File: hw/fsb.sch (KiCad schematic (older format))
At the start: 11 parts, among them J101 AMPSEAL_8_POS_VERT_WHITE_SEAL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, J102 AMPSEAL_23_POS_VERT_WHITE_SEA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

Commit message: last modifications to 3.0.0
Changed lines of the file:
@@
 F21 "DOORSW2" I L 4250 5050 60
 F22 "SEATSW" I L 4250 4700 60
+F23 "HEATER_PWM" O R 6400 5200 50
 $EndSheet
 $Comp
@@
 Text Label 9550 5200 0    50   ~ 0
 HEATER_15-
+Wire Wire Line
+	6400 5200 8500 5200
 $EndSCHEMATC

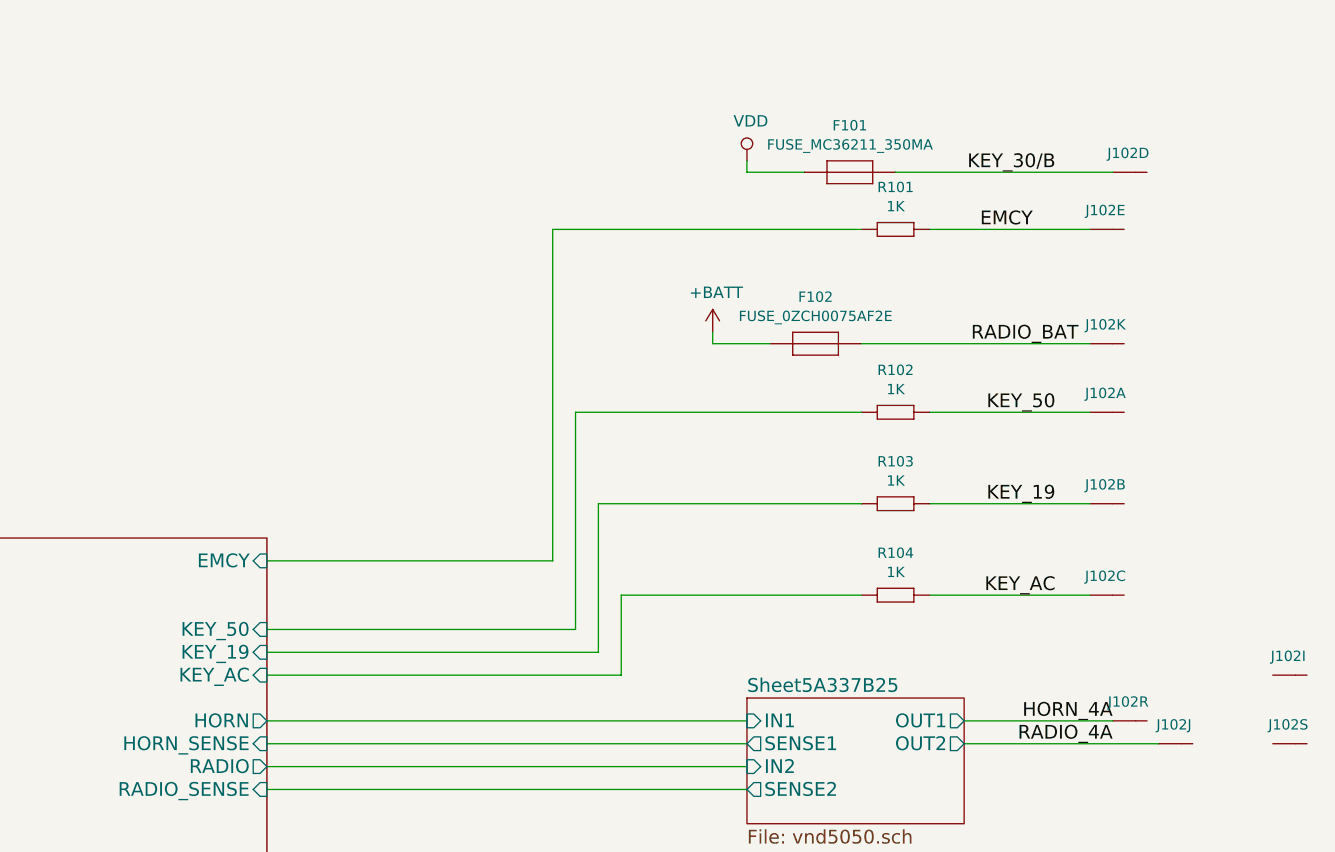
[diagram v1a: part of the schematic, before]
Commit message: hw 3.1.0 created. Fuel level moved from esb to fsb
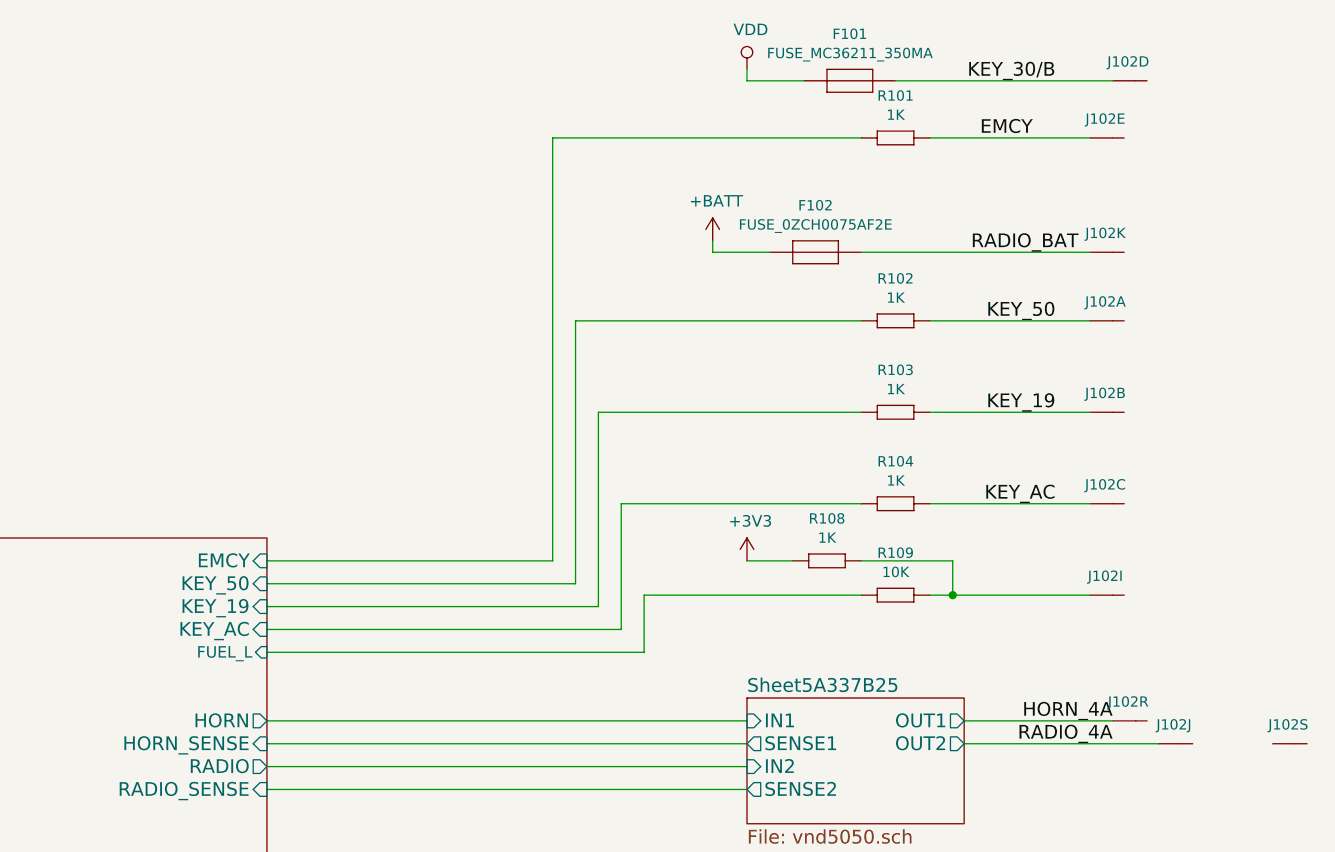
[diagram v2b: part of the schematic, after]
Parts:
- added R108: 1K, yageo:0603, symbol fsb-rescue:1K
- added R109: 10K, yageo:0603, symbol fsb-rescue:10K
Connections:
- net +3V3: now also R108.1 (R1)
- net at J102.P$9 (S): now also R108.2 (R2), R109.1 (R1)
- new net LPC1549/FUEL_L: R109.2 (R2)
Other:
- moved on the sheet: F101, F102, J102A, J102B, J102C, J102D, J102E, J102I, J102K, R101, R102, R103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

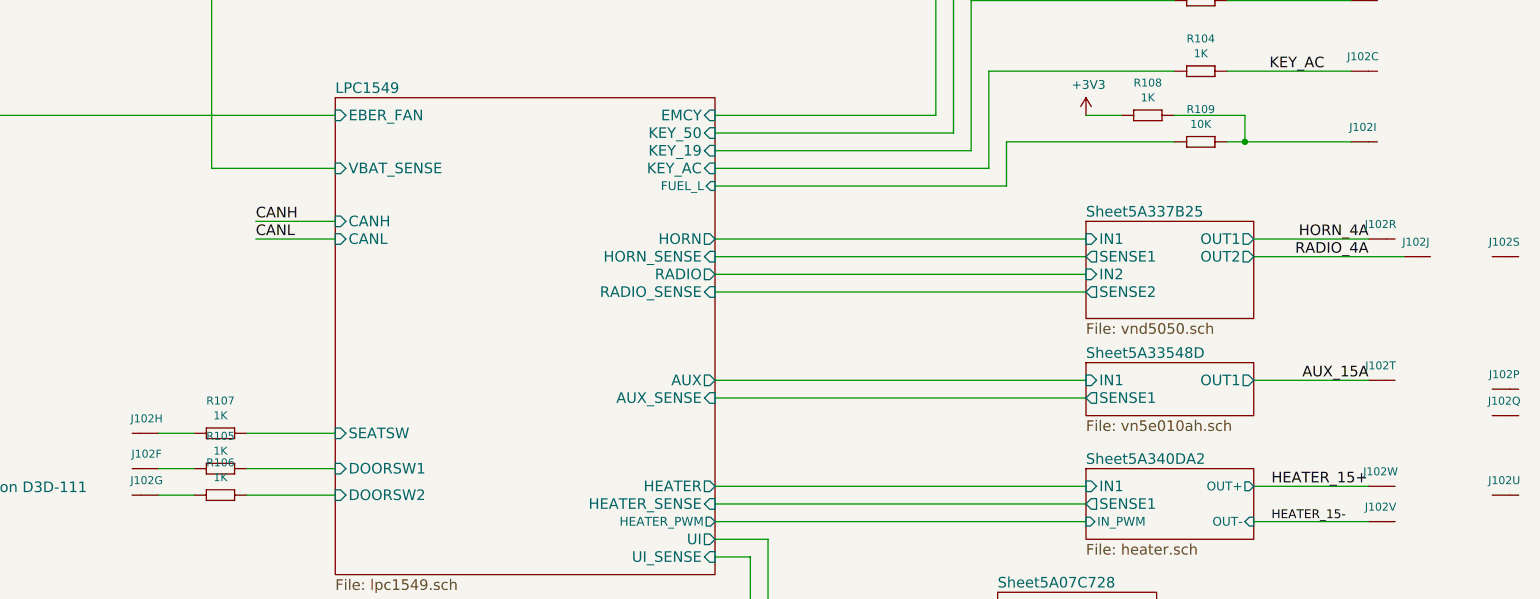
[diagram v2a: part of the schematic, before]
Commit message: 4.1.0 pcb ordered, with modified flyback diodes
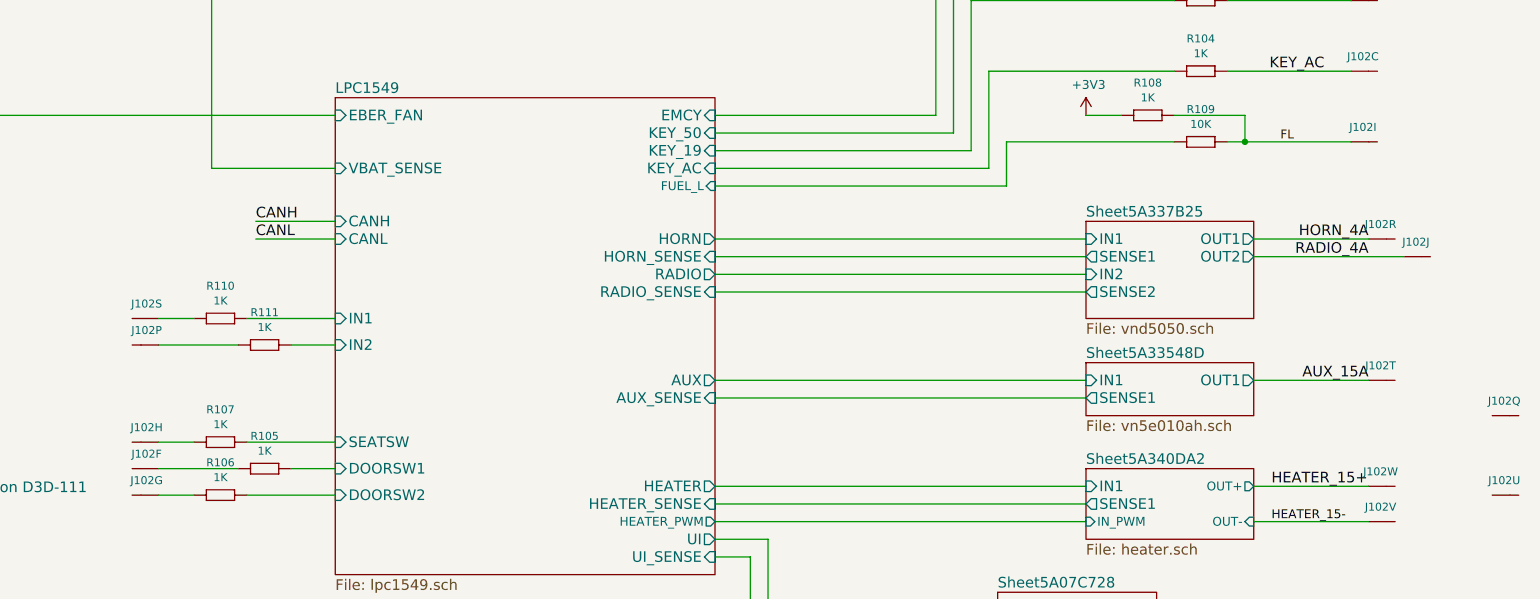
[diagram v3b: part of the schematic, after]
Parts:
- added R110, R111: 1K, yageo:0603, symbol fsb-rescue:1K
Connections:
- net FL: now reaches J102.P$9 (S), R108.2 (R2), R109.1 (R1)
- net at J102.P$16 (S): now also R111.2 (R2)
- net at J102.P$19 (S): now also R110.2 (R2)
- new net LPC1549/IN1: R110.1 (R1)
- new net LPC1549/IN2: R111.1 (R1)
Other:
- moved on the sheet: J102H, J102P, J102S, R105, R107
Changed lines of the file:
@@
 F20 "DOORSW1" I L 4250 4900 60
 F21 "DOORSW2" I L 4250 5050 60
-F22 "SEATSW" I L 4250 4700 60
+F22 "SEATSW" I L 4250 4750 60
 F23 "HEATER_PWM" O R 6400 5200 50
 F24 "FUEL_L" I R 6400 3300 50
+F25 "IN1" I L 4250 4050 60
+F26 "IN2" I L 4250 4200 60
 $EndSheet
 $Comp
@@
 L fsb-rescue:AMPSEAL_23_POS_VERT_WHITE_SEALED_1-776228-2-RESCUE-fsb J102
 U 8 1 5988B38C
-P 3150 4700
-F 0 "J102" H 3118 4783 45  0000 C CNN
-F 1 "AMPSEAL_23_POS_VERT_WHITE_SEALED_1-776228-2" H 3150 4700 45  0001 L BNN
-F 2 "usevolt:AMPSEAL_23_POS_776200-1" H 3180 4850 20  0001 C CNN
-F 3 "http://www.mouser.com/ds/2/418/NG_CD_776228_C13-692101.pdf" H 3250 4670 60  0001 C CNN
-F 4 "571-1-776228-2" H 3650 5070 60  0001 C CNN "1st Source Part Number"
-F 5 "1-776228-2" H 3450 4870 60  0001 C CNN "Manufacturer Part Number"
-F 6 "Mouser" H 3550 4970 60  0001 C CNN "1st Source"
-F 7 "TE Connectivity" H 3350 4770 60  0001 C CNN "Manufacturer"
-	8    3150 4700
+P 3150 4750
+F 0 "J102" H 3118 4833 45  0000 C CNN
+F 1 "AMPSEAL_23_POS_VERT_WHITE_SEALED_1-776228-2" H 3150 4750 45  0001 L BNN
+F 2 "usevolt:AMPSEAL_23_POS_776200-1" H 3180 4900 20  0001 C CNN
+F 3 "http://www.mouser.com/ds/2/418/NG_CD_776228_C13-692101.pdf" H 3250 4720 60  0001 C CNN
+F 4 "571-1-776228-2" H 3650 5120 60  0001 C CNN "1st Source Part Number"
+F 5 "1-776228-2" H 3450 4920 60  0001 C CNN "Manufacturer Part Number"
+F 6 "Mouser" H 3550 5020 60  0001 C CNN "1st Source"
+F 7 "TE Connectivity" H 3350 4820 60  0001 C CNN "Manufacturer"
+	8    3150 4750
 	-1   0    0    -1
 $EndComp
@@
 L fsb-rescue:AMPSEAL_23_POS_VERT_WHITE_SEALED_1-776228-2-RESCUE-fsb J102
 U 16 1 5988B7B4
-P 10900 4450
-F 0 "J102" H 10868 4533 45  0000 C CNN
-F 1 "AMPSEAL_23_POS_VERT_WHITE_SEALED_1-776228-2" H 10900 4450 45  0001 L BNN
-F 2 "usevolt:AMPSEAL_23_POS_776200-1" H 10930 4600 20  0001 C CNN
-F 3 "http://www.mouser.com/ds/2/418/NG_CD_776228_C13-692101.pdf" H 11000 4420 60  0001 C CNN
-F 4 "571-1-776228-2" H 11400 4820 60  0001 C CNN "1st Source Part Number"
-F 5 "1-776228-2" H 11200 4620 60  0001 C CNN "Manufacturer Part Number"
-F 6 "Mouser" H 11300 4720 60  0001 C CNN "1st Source"
-F 7 "TE Connectivity" H 11100 4520 60  0001 C CNN "Manufacturer"
-	16   10900 4450
-	1    0    0    -1
+P 3150 4200
+F 0 "J102" H 3118 4283 45  0000 C CNN
+F 1 "AMPSEAL_23_POS_VERT_WHITE_SEALED_1-776228-2" H 3150 4200 45  0001 L BNN
+F 2 "usevolt:AMPSEAL_23_POS_776200-1" H 3180 4350 20  0001 C CNN
+F 3 "http://www.mouser.com/ds/2/418/NG_CD_776228_C13-692101.pdf" H 3250 4170 60  0001 C CNN
+F 4 "571-1-776228-2" H 3650 4570 60  0001 C CNN "1st Source Part Number"
+F 5 "1-776228-2" H 3450 4370 60  0001 C CNN "Manufacturer Part Number"
+F 6 "Mouser" H 3550 4470 60  0001 C CNN "1st Source"
+F 7 "TE Connectivity" H 3350 4270 60  0001 C CNN "Manufacturer"
+	16   3150 4200
+	-1   0    0    -1
 $EndComp
 $Comp
@@
 L fsb-rescue:AMPSEAL_23_POS_VERT_WHITE_SEALED_1-776228-2-RESCUE-fsb J102
 U 19 1 5988C267
-P 10900 3700
-F 0 "J102" H 10868 3783 45  0000 C CNN
-F 1 "AMPSEAL_23_POS_VERT_WHITE_SEALED_1-776228-2" H 10900 3700 45  0001 L BNN
-F 2 "usevolt:AMPSEAL_23_POS_776200-1" H 10930 3850 20  0001 C CNN
-F 3 "http://www.mouser.com/ds/2/418/NG_CD_776228_C13-692101.pdf" H 11000 3670 60  0001 C CNN
-F 4 "571-1-776228-2" H 11400 4070 60  0001 C CNN "1st Source Part Number"
-F 5 "1-776228-2" H 11200 3870 60  0001 C CNN "Manufacturer Part Number"
-F 6 "Mouser" H 11300 3970 60  0001 C CNN "1st Source"
-F 7 "TE Connectivity" H 11100 3770 60  0001 C CNN "Manufacturer"
-	19   10900 3700
-	1    0    0    -1
+P 3150 4050
+F 0 "J102" H 3118 4133 45  0000 C CNN
+F 1 "AMPSEAL_23_POS_VERT_WHITE_SEALED_1-776228-2" H 3150 4050 45  0001 L BNN
+F 2 "usevolt:AMPSEAL_23_POS_776200-1" H 3180 4200 20  0001 C CNN
+F 3 "http://www.mouser.com/ds/2/418/NG_CD_776228_C13-692101.pdf" H 3250 4020 60  0001 C CNN
+F 4 "571-1-776228-2" H 3650 4420 60  0001 C CNN "1st Source Part Number"
+F 5 "1-776228-2" H 3450 4220 60  0001 C CNN "Manufacturer Part Number"
+F 6 "Mouser" H 3550 4320 60  0001 C CNN "1st Source"
+F 7 "TE Connectivity" H 3350 4120 60  0001 C CNN "Manufacturer"
+	19   3150 4050
+	-1   0    0    -1
 $EndComp
 $Comp
@@
 	4250 5050 3750 5050
 Wire Wire Line
-	3750 4900 4250 4900
+	4000 4900 4250 4900
 $Comp
 L fsb-rescue:1K R105
 U 1 1 5A09BE6F
-P 3550 4900
-F 0 "R105" H 3600 5084 45  0000 C CNN
-F 1 "1K" H 3600 5000 45  0000 C CNN
-F 2 "yageo:0603" H 3580 5050 20  0001 C CNN
-F 3 "" H 3519 4939 60  0001 C CNN
-F 4 "" H 3919 5339 60  0001 C CNN "1st Source Part Number"
-F 5 "Digikey" H 3819 5239 60  0001 C CNN "1st Source"
-F 6 "RC0603FR-071KL" H 3719 5139 60  0001 C CNN "Manufacturer Part Number"
-F 7 "YAGEO" H 3619 5039 60  0001 C CNN "Manufacturer"
-	1    3550 4900
+P 3800 4900
+F 0 "R105" H 3850 5084 45  0000 C CNN
+F 1 "1K" H 3850 5000 45  0000 C CNN
+F 2 "yageo:0603" H 3830 5050 20  0001 C CNN
+F 3 "" H 3769 4939 60  0001 C CNN
+F 4 "" H 4169 5339 60  0001 C CNN "1st Source Part Number"
+F 5 "Digikey" H 4069 5239 60  0001 C CNN "1st Source"
+F 6 "RC0603FR-071KL" H 3969 5139 60  0001 C CNN "Manufacturer Part Number"
+F 7 "YAGEO" H 3869 5039 60  0001 C CNN "Manufacturer"
+	1    3800 4900
 	1    0    0    -1
 $EndComp
@@
 $EndComp
 Wire Wire Line
-	3450 4900 3250 4900
+	3700 4900 3250 4900
 Wire Wire Line
 	3250 5050 3450 5050
@@
 $EndSheet
 Wire Wire Line
-	3750 4700 4250 4700
+	3750 4750 4250 4750
 $Comp
 L fsb-rescue:1K R107
 U 1 1 5A33C203
-P 3550 4700
-F 0 "R107" H 3600 4884 45  0000 C CNN
-F 1 "1K" H 3600 4800 45  0000 C CNN
-F 2 "yageo:0603" H 3580 4850 20  0001 C CNN
-F 3 "" H 3519 4739 60  0001 C CNN
-F 4 "" H 3919 5139 60  0001 C CNN "1st Source Part Number"
-F 5 "Digikey" H 3819 5039 60  0001 C CNN "1st Source"
-F 6 "RC0603FR-071KL" H 3719 4939 60  0001 C CNN "Manufacturer Part Number"
-F 7 "YAGEO" H 3619 4839 60  0001 C CNN "Manufacturer"
-	1    3550 4700
-	1    0    0    -1
-$EndComp
-Wire Wire Line
-	3450 4700 3250 4700
+P 3550 4750
+F 0 "R107" H 3600 4934 45  0000 C CNN
+F 1 "1K" H 3600 4850 45  0000 C CNN
+F 2 "yageo:0603" H 3580 4900 20  0001 C CNN
+F 3 "" H 3519 4789 60  0001 C CNN
+F 4 "" H 3919 5189 60  0001 C CNN "1st Source Part Number"
+F 5 "Digikey" H 3819 5089 60  0001 C CNN "1st Source"
+F 6 "RC0603FR-071KL" H 3719 4989 60  0001 C CNN "Manufacturer Part Number"
+F 7 "YAGEO" H 3619 4889 60  0001 C CNN "Manufacturer"
+	1    3550 4750
+	1    0    0    -1
+$EndComp
+Wire Wire Line
+	3450 4750 3250 4750
 $Sheet
 S 8500 4900 950  400
@@
 Wire Wire Line
 	8050 3050 9000 3050
+Text Label 9600 3050 0    50   ~ 0
+FL
+$Comp
+L fsb-rescue:1K R111
+U 1 1 5B1711B4
+P 3800 4200
+F 0 "R111" H 3850 4384 45  0000 C CNN
+F 1 "1K" H 3850 4300 45  0000 C CNN
+F 2 "yageo:0603" H 3830 4350 20  0001 C CNN
+F 3 "" H 3769 4239 60  0001 C CNN
+F 4 "" H 4169 4639 60  0001 C CNN "1st Source Part Number"
+F 5 "Digikey" H 4069 4539 60  0001 C CNN "1st Source"
+F 6 "RC0603FR-071KL" H 3969 4439 60  0001 C CNN "Manufacturer Part Number"
+F 7 "YAGEO" H 3869 4339 60  0001 C CNN "Manufacturer"
+	1    3800 4200
+	1    0    0    -1
+$EndComp
+$Comp
+L fsb-rescue:1K R110
+U 1 1 5B1712C5
+P 3550 4050
+F 0 "R110" H 3600 4234 45  0000 C CNN
+F 1 "1K" H 3600 4150 45  0000 C CNN
+F 2 "yageo:0603" H 3580 4200 20  0001 C CNN
+F 3 "" H 3519 4089 60  0001 C CNN
+F 4 "" H 3919 4489 60  0001 C CNN "1st Source Part Number"
+F 5 "Digikey" H 3819 4389 60  0001 C CNN "1st Source"
+F 6 "RC0603FR-071KL" H 3719 4289 60  0001 C CNN "Manufacturer Part Number"
+F 7 "YAGEO" H 3619 4189 60  0001 C CNN "Manufacturer"
+	1    3550 4050
+	1    0    0    -1
+$EndComp
+Wire Wire Line
+	4250 4050 3750 4050
+Wire Wire Line
+	4000 4200 4250 4200
+Wire Wire Line
+	3250 4050 3450 4050
+Wire Wire Line
+	3700 4200 3250 4200
 $EndSCHEMATC

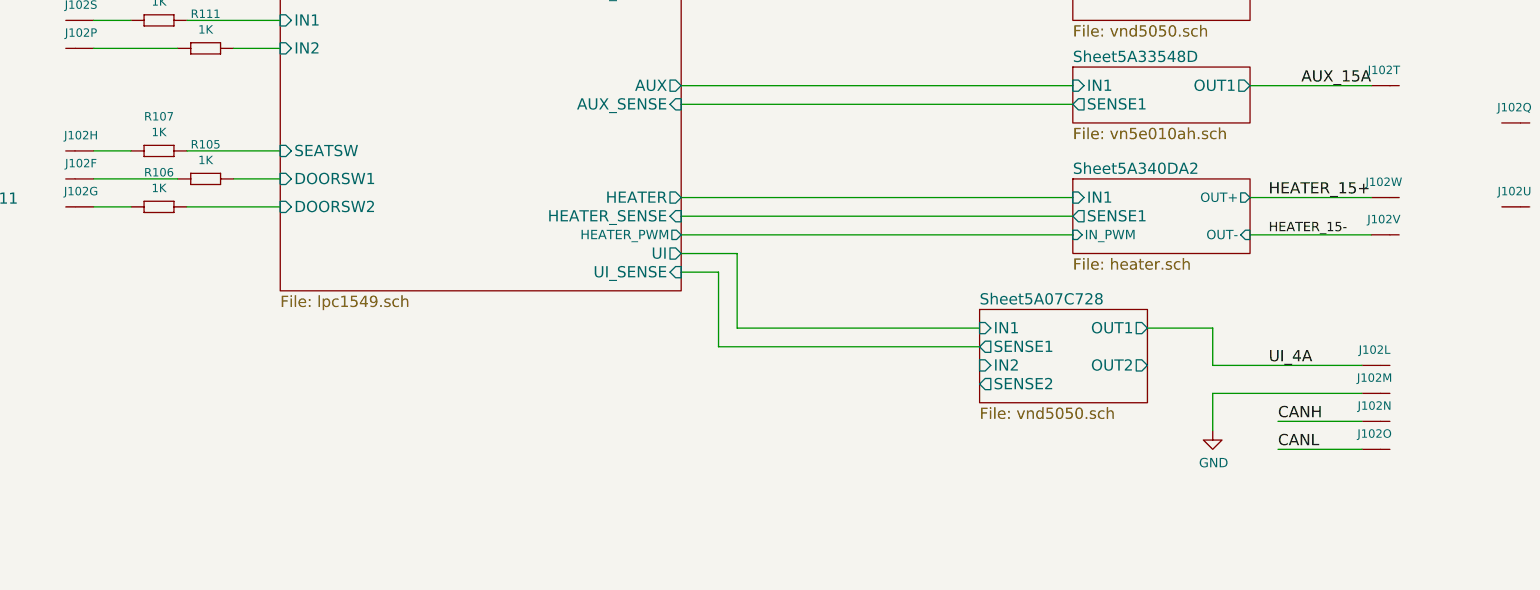
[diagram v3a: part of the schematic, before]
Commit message: hw 6.0.0 created, fits uw aluminium enclosure
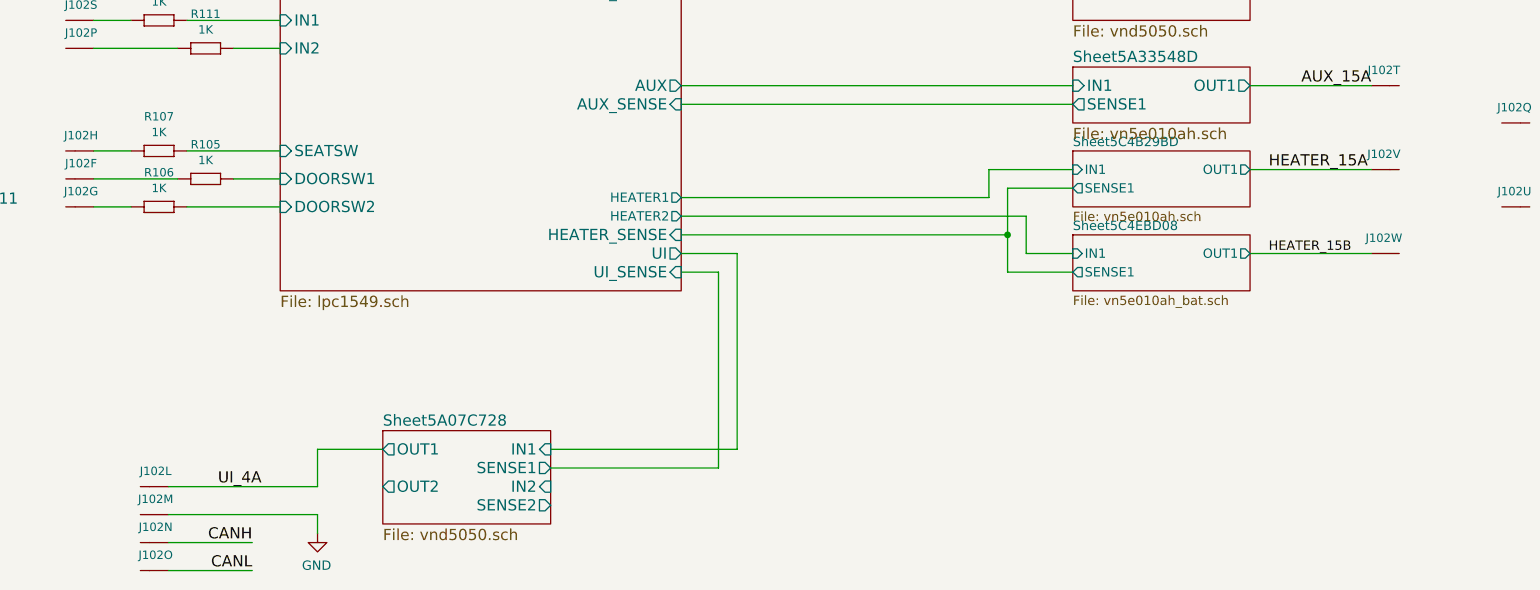
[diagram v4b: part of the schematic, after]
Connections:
- net HEATER_15+ renamed HEATER_15B
- net HEATER_15- renamed HEATER_15A
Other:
- moved on the sheet: J102L, J102M, J102N, J102O, J102V, J102W
